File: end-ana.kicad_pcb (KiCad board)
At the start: 2 copper layers, 160 x 80 mm, 10 parts

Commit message: Contact pads.  Shuffle the big cap.
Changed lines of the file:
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@@
+			(thermal_bridge_angle 90)
+		)
+		(pad "1" smd circle
+			(at 0 0)
+			(size 10 10)
+			(layers "F.Cu" "F.Mask")
+			(net 6 "/Gnd")
+			(pinfunction "1")
+			(pintype "input")
 			(thermal_bridge_angle 90)
 		)
@@
 			(thermal_bridge_angle 90)
 		)
+		(pad "1" smd circle
+			(at 0 0)
+			(size 10 10)
+			(layers "F.Cu" "F.Mask")
+			(net 7 "/Bbuf")
+			(pinfunction "1")
+			(pintype "input")
+			(thermal_bridge_angle 90)
+		)
 		(embedded_fonts no)
 	)
@@
 			(thermal_bridge_angle 90)
 		)
+		(pad "1" smd circle
+			(at 0 0)
+			(size 10 10)
+			(layers "F.Cu" "F.Mask")
+			(net 4 "/Abuf")
+			(pinfunction "1")
+			(pintype "input")
+			(thermal_bridge_angle 90)
+		)
 		(embedded_fonts no)
 	)
@@
 			(thermal_bridge_angle 90)
 		)
+		(pad "1" smd circle
+			(at 0 0)
+			(size 10 10)
+			(layers "F.Cu" "F.Mask")
+			(net 2 "/A")
+			(pinfunction "1")
+			(pintype "input")
+			(thermal_bridge_angle 90)
+		)
 		(embedded_fonts no)
 	)
@@
 			(thermal_bridge_angle 90)
 		)
+		(pad "1" smd circle
+			(at 0 0)
+			(size 10 10)
+			(layers "F.Cu" "F.Mask")
+			(net 3 "/B")
+			(pinfunction "1")
+			(pintype "input")
+			(thermal_bridge_angle 90)
+		)
 		(embedded_fonts no)
 	)
@@
 			(thermal_bridge_angle 90)
 		)
+		(pad "1" smd circle
+			(at 0 0)
+			(size 10 10)
+			(layers "F.Cu" "F.Mask")
+			(net 5 "/Sum")
+			(pinfunction "1")
+			(pintype "input")
+			(thermal_bridge_angle 90)
+		)
 		(embedded_fonts no)
 	)
-	(gr_circle
-		(center 119.85 67.45)
-		(end 124.85 67.45)
+	(gr_rect
+		(start 128 72)
+		(end 132 74)
 		(stroke
 			(width 0)
@@
 		)
 		(fill yes)
-		(layer "F.Cu")
-		(net 6)
-	)
-	(gr_circle
-		(center 214.85 67.45)
-		(end 219.85 67.45)
-		(stroke
-			(width 0)
-			(type default)
-		)
-		(fill yes)
-		(layer "F.Cu")
-		(net 3)
-	)
-	(gr_circle
-		(center 176.85 67.45)
-		(end 181.85 67.45)
-		(stroke
-			(width 0)
-			(type default)
-		)
-		(fill yes)
-		(layer "F.Cu")
-		(net 7)
-	)
-	(gr_circle
-		(center 195.85 67.45)
-		(end 200.85 67.45)
-		(stroke
-			(width 0)
-			(type default)
-		)
-		(fill yes)
-		(layer "F.Cu")
-		(net 2)
-	)
-	(gr_circle
-		(center 138.8 67.45)
-		(end 143.8 67.45)
-		(stroke
-			(width 0)
-			(type default)
-		)
-		(fill yes)
-		(layer "F.Cu")
-		(net 5)
-	)
-	(gr_circle
-		(center 157.85 67.45)
-		(end 162.85 67.45)
-		(stroke
-			(width 0)
-			(type default)
-		)
-		(fill yes)
-		(layer "F.Cu")
-		(net 4)
+		(layer "B.Mask")
 	)
 	(gr_arc
@@
 		(net 1)
 		(net_name "GNDPWR")
-		(locked yes)
 		(layers "F.Cu" "B.Cu")
 		(name "Gnd")
@@
 		(polygon
 			(pts
-				(xy 65 55) (xy 235 55) (xy 235 170) (xy 65 170)
+				(xy 65 55) (xy 235 55) (xy 235 145) (xy 65 145)
 			)
 		)
@@
 		(net 0)
 		(net_name "")
+		(locked yes)
 		(layer "B.Mask")
 		(name "Earth")

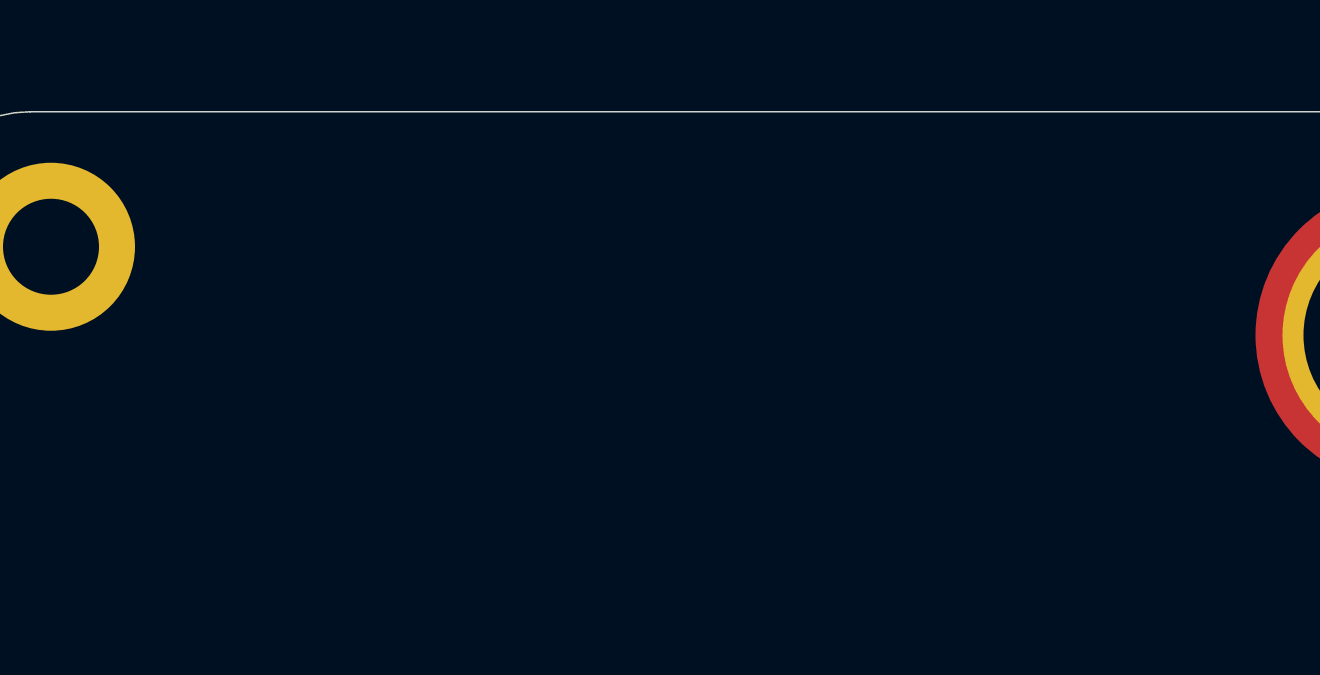
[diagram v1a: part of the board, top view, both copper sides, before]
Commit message: Change some footprints.
Mounting holes for covers.
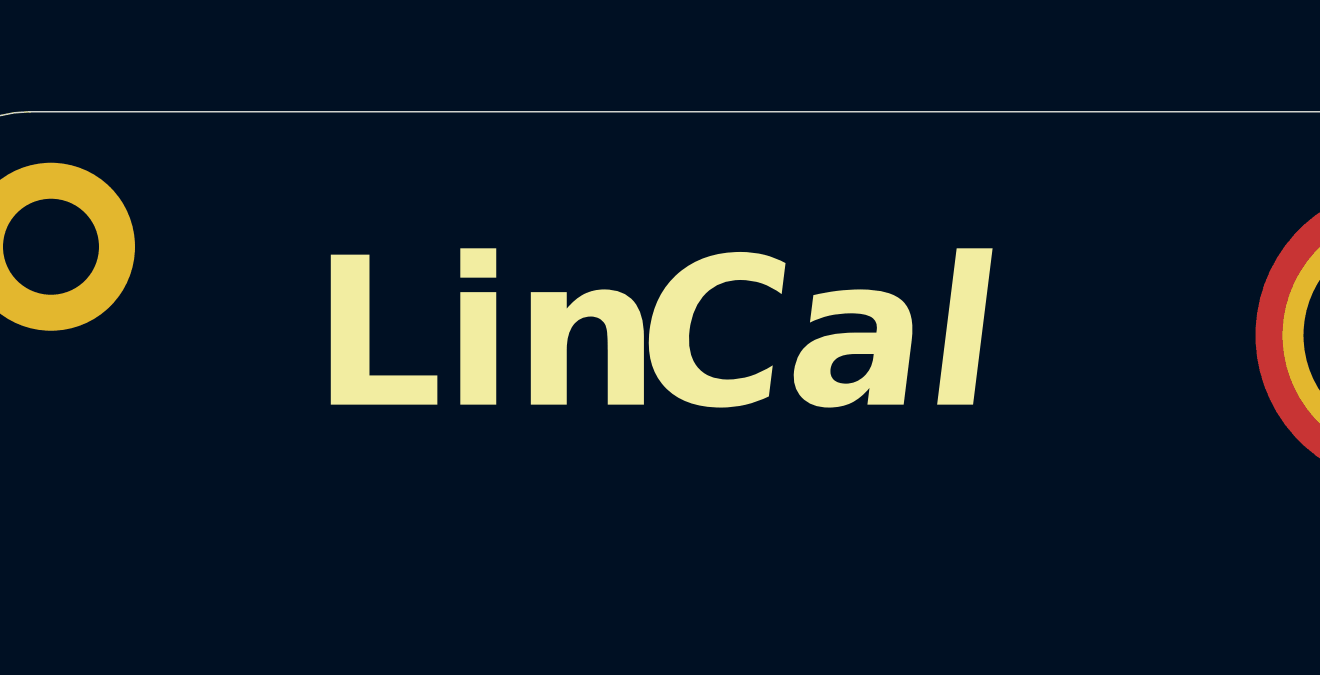
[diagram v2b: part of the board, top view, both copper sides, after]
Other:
- board text added: "Cal"
- board text added: "Lin"
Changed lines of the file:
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@@
 		(layer "User.1")
+	)
+	(gr_text "Lin"
+		(at 95 67.45 0)
+		(layer "F.SilkS")
+		(effects
+			(font
+				(size 5 5)
+				(thickness 1)
+				(bold yes)
+			)
+			(justify right)
+		)
+	)
+	(gr_text "Cal"
+		(at 94 67.45 0)
+		(layer "F.SilkS")
+		(effects
+			(font
+				(size 5 5)
+				(thickness 1)
+				(bold yes)
+				(italic yes)
+			)
+			(justify left)
+		)
 	)
 	(dimension
